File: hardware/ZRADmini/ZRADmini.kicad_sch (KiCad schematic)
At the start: 57 parts, among them J1 Conn_Coaxial, J2 Qwiic_RA, J3 Conn_Coaxial, J4 Conn_02x05_Odd_Even, J5 Conn_01x02, J6 Conn_01x05, J7 Conn_01x05, J8 USB_C_Receptacle_USB2.0_16P, SW1 PTS810, SW2 PTS810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

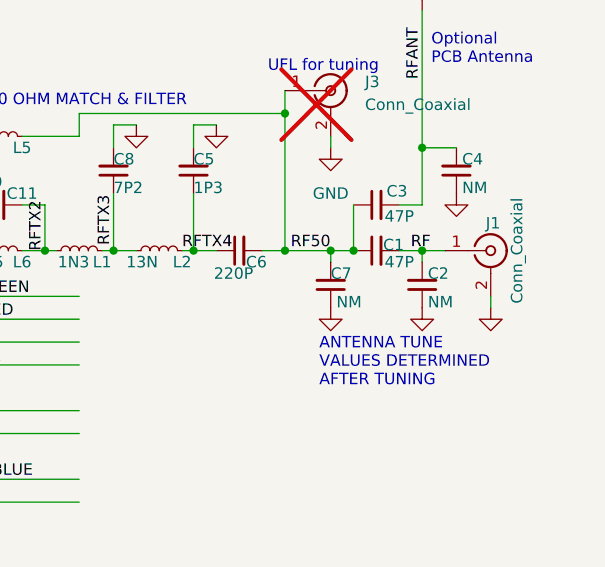
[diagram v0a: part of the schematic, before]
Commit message: add RF Range test data and 3D programming jig
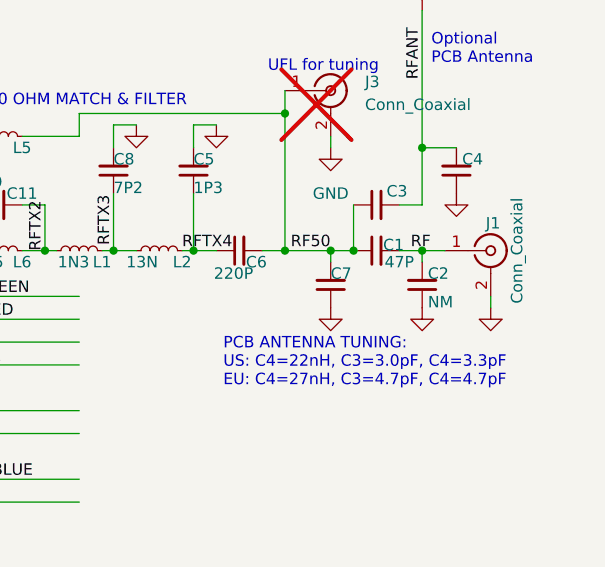
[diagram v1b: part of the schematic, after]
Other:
- note added: "PCB ANTENNA TUNING: US: C4=22nH, C3=3.0pF, C4=3.3pF EU: C4=27nH, C3=4.7pF, C4=4.7pF"
- note removed: "ANTENNA TUNE VALUES DETERMINED AFTER TUNING"
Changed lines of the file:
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@@
 	(title_block
 		(title "ZRAD Mini Z-Wave  Reference Application Design")
-		(date "2024-11-13")
-		(rev "A")
+		(date "2024-12-18")
+		(rev "A1")
 		(company "Z-Wave Alliance")
 	)
@@
 		)
 	)
-	(text "ANTENNA TUNE\nVALUES DETERMINED\nAFTER TUNING"
+	(text "PCB ANTENNA TUNING:\nUS: C4=22nH, C3=3.0pF, C4=3.3pF\nEU: C4=27nH, C3=4.7pF, C4=4.7pF"
 		(exclude_from_sim no)
-		(at 240.03 111.76 0)
+		(at 229.362 111.76 0)
 		(effects
 			(font
@@
 				)
 				(justify right)
+				(hide yes)
 			)
 		)
@@
 					(size 1.27 1.27)
 				)
+				(hide yes)
 			)
 		)
@@
 				)
 				(justify right)
+				(hide yes)
 			)
 		)
